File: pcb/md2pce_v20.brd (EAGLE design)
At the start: 84.7 x 70.1 mm, 17 parts, among them IC1 74HC157N, IC2 74HC157N, IC3 74HC157N, IC4 4163N

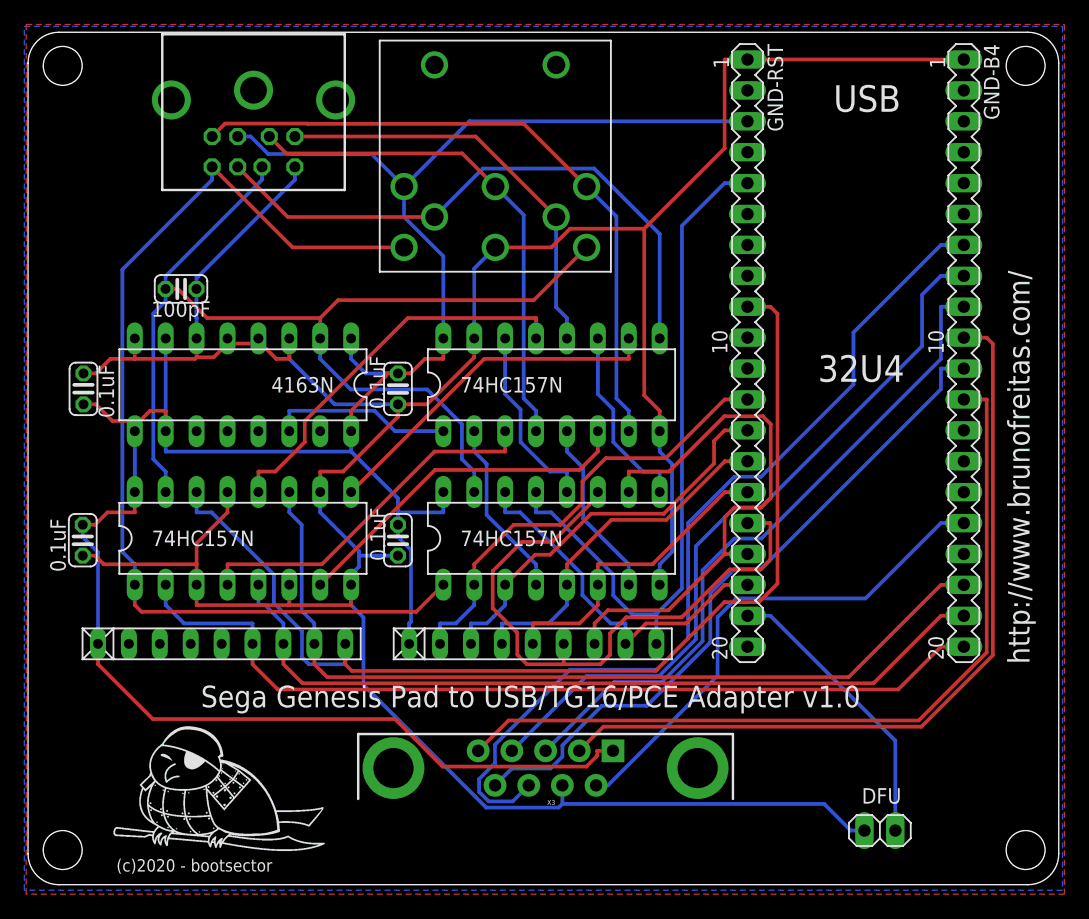
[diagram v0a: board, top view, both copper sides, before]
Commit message: PCB version 2.0 (using CPLD). Added Quartus project files.
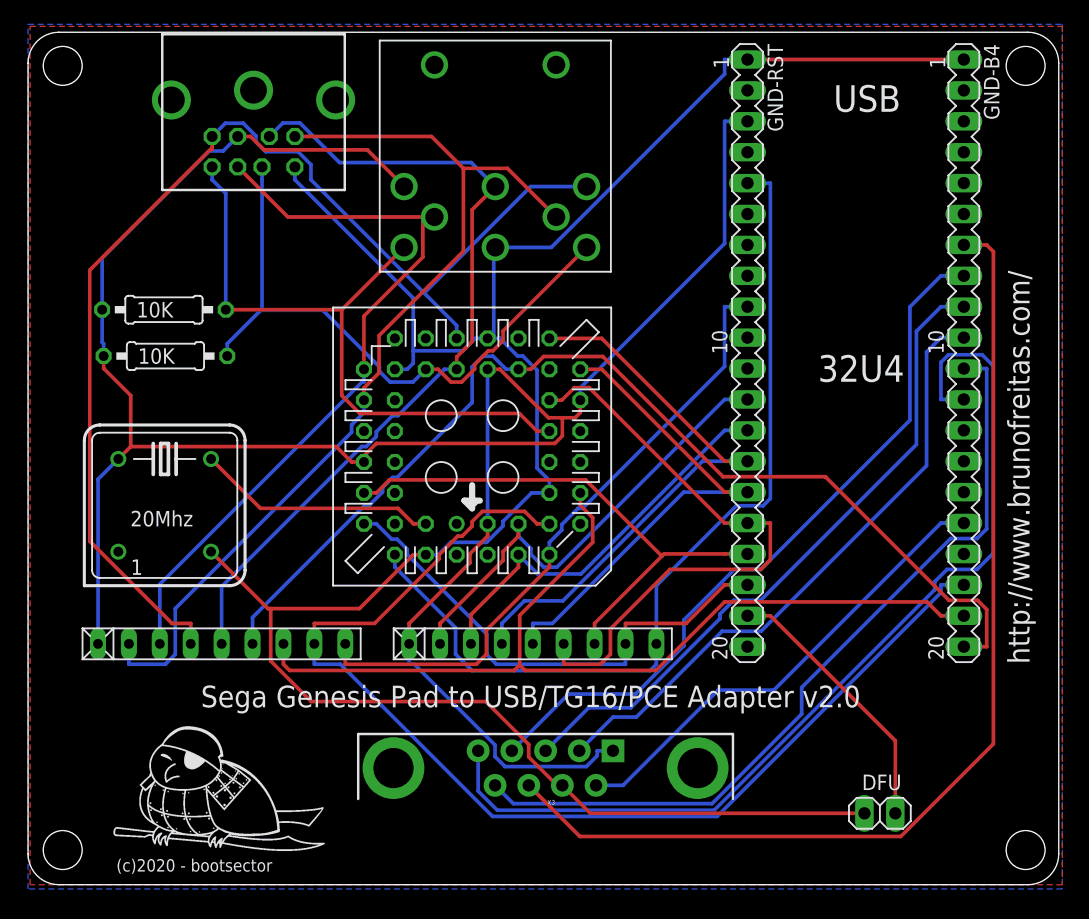
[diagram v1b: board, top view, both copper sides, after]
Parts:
- removed C1, C2, C3, C4: 0.1uF, rcl:C025-024X044
- removed C5: 100pF, rcl:C025-024X044
- removed IC1, IC2, IC3: 74HC157N, 74xx-eu:DIL16
- removed IC4: 4163N, 40xx:DIL16
- added IC6: EPM7064S44, altera:PLCC-S44
- added QG1: 20Mhz, crystal:DIL08S
- added R1, R2: 10K, rcl:0207/10
- moved JP1 1.42 mm to (70.0, 5.87)
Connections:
- removed net N$1: IC1.4, IC3.3
- removed net N$2: IC1.7, IC3.6
- removed net N$3: IC1.9, IC3.10
- removed net N$4: IC1.12, IC3.13
- removed net N$5: IC2.4, IC3.2
- removed net N$6: IC2.7, IC3.5
- removed net N$7: IC2.9, IC3.11
- removed net N$8: IC2.12, IC3.14
- removed net N$9: IC3.1, IC4.14
- new net GCLK: IC6.43, QG1.5
- new net TCK: IC6.32
- new net TDI: IC6.7
- new net TDO: IC6.38
- new net TMS: IC6.13
- net B0: now also IC6.40; no longer IC2.13
- net B4: now also IC6.21; no longer IC1.2
- net B5: now also IC6.9; no longer IC1.5
- net B6: now also IC6.8; no longer IC1.11
- net B7: now also IC6.6; no longer IC1.14
- net D0: now also IC6.5; no longer IC2.2
- net D1: now also IC6.4; no longer IC2.3
- net D2: now also IC6.18; no longer IC2.5
- net D3: now also IC6.17; no longer IC2.6
- net D4: now also IC6.16; no longer IC2.11
- net D5: now also IC6.37; no longer IC2.10
- net D6: now also IC6.39; no longer IC2.14
- net DIN2: now also IC6.25, RN1.5; no longer IC3.4
- net DIN3: now also IC6.24, RN1.4; no longer IC3.7
- net DIN4: now also IC6.29, RN1.3; no longer IC3.9
- net DIN5: now also IC6.31, RN1.2; no longer IC3.12
- net DIN6: now also IC6.14, R1.2; no longer IC1.1, IC2.1
- net DIN7: now also IC6.27, R2.2; no longer C5.1, IC1.15, IC2.15, IC4.2
- net GND: now also IC6.10, IC6.22, IC6.30, IC6.42, QG1.4; no longer C1.2, C2.2, C3.2, C4.2, C5.2, IC1.10, IC1.13, IC1.3, IC1.6, IC1.8, IC2.8, IC3.15, IC3.8, IC4.3, IC4.4, IC4.5, IC4.6, IC4.8
- net VCC: now also IC6.15, IC6.23, IC6.3, IC6.35, QG1.8, R1.1, R2.1; no longer C1.1, C2.1, C3.1, C4.1, IC1.16, IC2.16, IC3.16, IC4.1, IC4.10, IC4.16, IC4.7, IC4.9
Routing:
- net GND: track 267.4 -> 190.0 mm
- net DIN5: track 34.6 -> 79.8 mm
- net DIN3: track 54.9 -> 96.8 mm
- net DIN7: track 92.1 -> 52.3 mm
- net B7: track 88.7 -> 52.4 mm
- net N$4: track 32.4 -> 0.00 mm
- net DIN6: track 84.5 -> 54.3 mm
- net N$1: track 30.0 -> 0.00 mm
- net N$2: track 29.0 -> 0.00 mm
- net N$3: track 29.0 -> 0.00 mm
- net DIN2: track 41.8 -> 69.2 mm
- net B6: track 72.0 -> 94.1 mm
- net GCLK: track 0.00 -> 19.9 mm
- net D2: track 29.4 -> 47.9 mm
- net VCC: track 208.3 -> 192.0 mm
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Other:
- board text added: "Sega Genesis Pad to USB/TG16/PCE Adapter v2.0"
- board text removed: "Sega Genesis Pad to USB/TG16/PCE Adapter v1.0"
